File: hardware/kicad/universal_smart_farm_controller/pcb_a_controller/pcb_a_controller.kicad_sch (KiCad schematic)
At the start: 55 parts, among them J1 Conn_01x12, J19 Conn_01x03, J2 Conn_01x03, J3 Conn_01x04, J4 Conn_01x04, J5 Conn_01x03, J6 Conn_01x03, J7 Conn_01x03, J8 Conn_01x03, J9 Conn_01x04, SW1 RESET, SW2 BOOT, U1 ESP32-WROOM-32E, U2 ADS1115IDGS, U3 MAX3485ESA+, U4 TPS5430DDA, U5 AP2112K-3.3

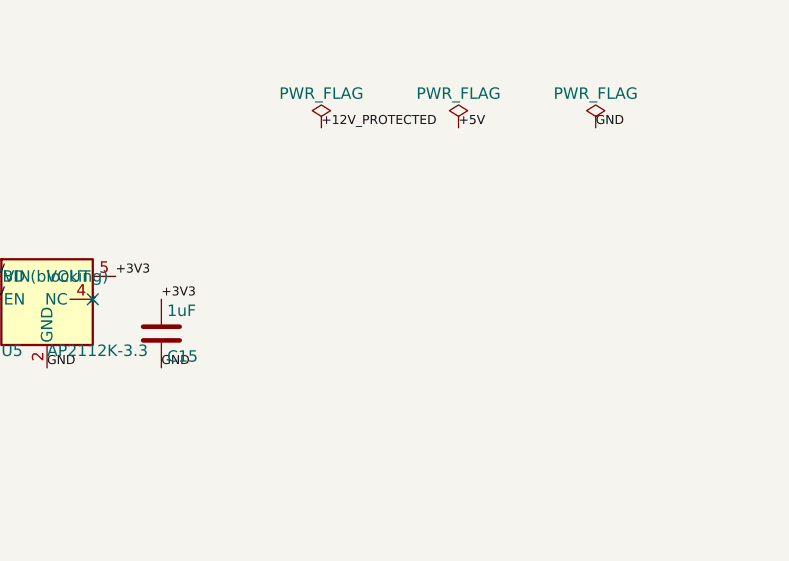
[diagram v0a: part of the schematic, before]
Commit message: Add supply and output LED circuits
Co-authored-by: tomnyle <175001228+tomnyle@users.noreply.github.com>
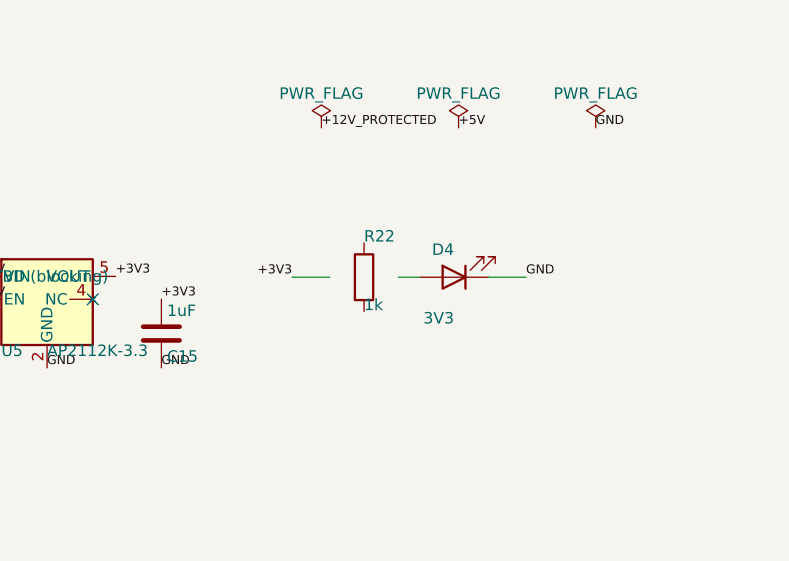
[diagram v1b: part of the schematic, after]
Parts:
- added D4: 3V3, LED_SMD:LED_0805_2012Metric, symbol Device:LED
- added R22: 1k, Resistor_SMD:R_0805_2012Metric, symbol Device:R
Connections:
- net GND: now also D4.1 (K)
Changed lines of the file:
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@@
 	)
 	(embedded_fonts no)
+	(symbol
+		(lib_id "Device:R")
+		(at 180.0000 42.0000 0)
+		(unit 1)
+		(exclude_from_sim no)
+		(in_bom yes)
+		(on_board yes)
+		(dnp no)
+		(fields_autoplaced no)
+		(property "Reference" "R22"
+			(at 180.0000 38.1900 0.0000)
+			(effects (font (size 1.27 1.27)) (justify left bottom))
+		)
+		(property "Value" "1k"
+			(at 180.0000 45.8100 0.0000)
+			(effects (font (size 1.27 1.27)) (justify left bottom))
+		)
+		(property "Footprint" "Resistor_SMD:R_0805_2012Metric"
+			(at 180.0000 42.0000 0.0000)
+			(effects (font (size 1.27 1.27)) (hide yes))
+		)
+		(pin "1")
+		(pin "2")
+		(instances
+			(project "pcb_a_controller"
+				(path "/ef6d9368-7a34-400f-be1a-9727cfacc43b" (reference "R22") (unit 1))
+			)
+		)
+	)
+	(symbol
+		(lib_id "Device:LED")
+		(at 190.0000 42.0000 180)
+		(unit 1)
+		(exclude_from_sim no)
+		(in_bom yes)
+		(on_board yes)
+		(dnp no)
+		(fields_autoplaced no)
+		(property "Reference" "D4"
+			(at 190.0000 38.1900 0.0000)
+			(effects (font (size 1.27 1.27)) (justify left bottom))
+		)
+		(property "Value" "3V3"
+			(at 190.0000 45.8100 0.0000)
+			(effects (font (size 1.27 1.27)) (justify left bottom))
+		)
+		(property "Footprint" "LED_SMD:LED_0805_2012Metric"
+			(at 190.0000 42.0000 0.0000)
+			(effects (font (size 1.27 1.27)) (hide yes))
+		)
+		(pin "1")
+		(pin "2")
+		(instances
+			(project "pcb_a_controller"
+				(path "/ef6d9368-7a34-400f-be1a-9727cfacc43b" (reference "D4") (unit 1))
+			)
+		)
+	)
+	(wire (pts (xy 172.0000 42.0000) (xy 176.1900 42.0000))
+		(stroke (width 0) (type default))
+	)
+	(wire (pts (xy 183.8100 42.0000) (xy 186.1900 42.0000))
+		(stroke (width 0) (type default))
+	)
+	(wire (pts (xy 193.8100 42.0000) (xy 198.0000 42.0000))
+		(stroke (width 0) (type default))
+	)
+	(label "+3V3"
+		(at 172.0000 42.0000 180)
+		(effects (font (size 1 1)) (justify right bottom))
+	)
+	(label "GND"
+		(at 198.0000 42.0000 0)
+		(effects (font (size 1 1)) (justify left bottom))
+	)
 )

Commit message: Wire WiFi, MQTT and ERROR status indicators
Co-authored-by: tomnyle <175001228+tomnyle@users.noreply.github.com>
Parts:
- added C16: 100nF, Capacitor_SMD:C_0805_2012Metric, symbol Device:C
- added D5: WIFI, LED_SMD:LED_0805_2012Metric, symbol Device:LED
- added D6: MQTT, LED_SMD:LED_0805_2012Metric, symbol Device:LED
- added D7: ERROR, LED_SMD:LED_0805_2012Metric, symbol Device:LED
- added R23, R24, R25: 1k, Resistor_SMD:R_0805_2012Metric, symbol Device:R
- added U: MCP23008, Package_SO:SOIC-18W_7.5x11.6mm_P1.27mm
- added U6: MCP23008, Package_SO:SOIC-18W_7.5x11.6mm_P1.27mm, symbol Microchip:MCP23008
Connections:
- new net ERROR_LED: D7.1 (K)
- new net MQTT_LED: D6.1 (K)
- new net WIFI_LED: D5.1 (K)
- no-connect marks 20 -> 27
